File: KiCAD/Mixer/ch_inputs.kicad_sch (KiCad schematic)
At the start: 0 parts

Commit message: Power Bus, Footprints, Audio Bus
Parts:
- added J1: AudioJack2, Eigene:TRS-BHT 3,5mm, symbol Connector_Audio:AudioJack2
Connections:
- net inputs_out: now also J1.T
- new net GND: J1.S

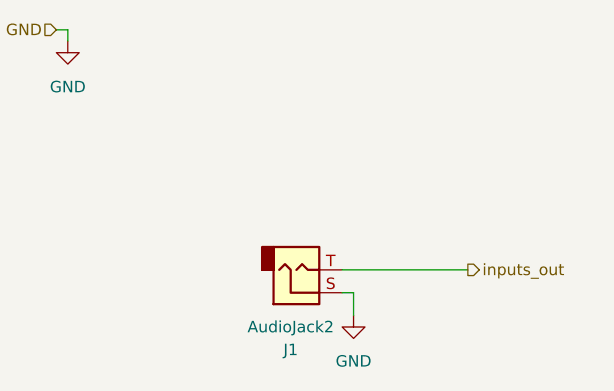
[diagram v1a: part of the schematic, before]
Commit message: added second channel and footprints / created PCB desing...might make PCB bit bigger
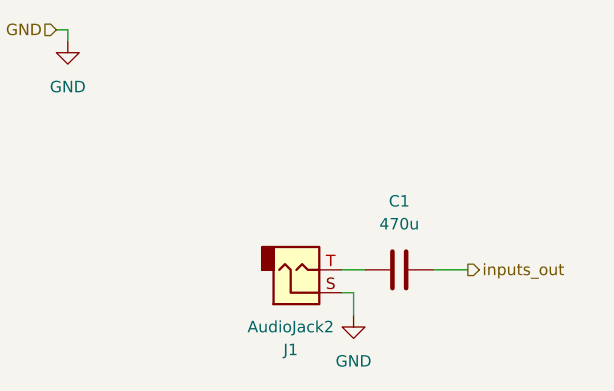
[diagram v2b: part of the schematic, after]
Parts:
- added C1: 470u, Capacitor_SMD:C_0805_2012Metric_Pad1.18x1.45mm_HandSolder, symbol Device:C
- J1: footprint Eigene:TRS-BHT 3,5mm -> Connector_Audio:Jack_3.5mm_QingPu_WQP-PJ398SM_Vertical_CircularHoles
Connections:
- net inputs_out: now also C1.2; no longer J1.T
- new net: C1.1, J1.T
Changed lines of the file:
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@@
 	(wire
 		(pts
-			(xy 58.42 50.8) (xy 72.39 50.8)
+			(xy 58.42 50.8) (xy 60.96 50.8)
 		)
 		(stroke
@@
 		(pts
 			(xy 27.94 24.13) (xy 27.94 25.4)
+		)
+		(stroke
+			(width 0)
+			(type default)
+		)
+	)
+	(wire
+		(pts
+			(xy 68.58 50.8) (xy 72.39 50.8)
 		)
 		(stroke
@@
 			)
 		)
-		(property "Footprint" "Eigene:TRS-BHT 3,5mm"
+		(property "Footprint" "Connector_Audio:Jack_3.5mm_QingPu_WQP-PJ398SM_Vertical_CircularHoles"
 			(at 53.34 50.8 0)
 			(hide yes)
@@
 		(instances
 			(project "Mixer"
+				(path "/322d427a-6aae-4762-92d6-d97688daf29b/8a2849b7-184d-4014-bb98-da9dec8b5f90/1134652d-8354-4f6a-9b2f-dc88b7881384"
+					(reference "J5")
+					(unit 1)
+				)
 				(path "/322d427a-6aae-4762-92d6-d97688daf29b/8a2849b7-184d-4014-bb98-da9dec8b5f90/ec5da5cc-7c1b-4e14-ac3c-00357a5f573e"
 					(reference "J1")
@@
 		(instances
 			(project "Mixer"
+				(path "/322d427a-6aae-4762-92d6-d97688daf29b/8a2849b7-184d-4014-bb98-da9dec8b5f90/1134652d-8354-4f6a-9b2f-dc88b7881384"
+					(reference "#PWR076")
+					(unit 1)
+				)
 				(path "/322d427a-6aae-4762-92d6-d97688daf29b/8a2849b7-184d-4014-bb98-da9dec8b5f90/ec5da5cc-7c1b-4e14-ac3c-00357a5f573e"
 					(reference "#PWR06")
+					(unit 1)
+				)
+			)
+		)
+	)
+	(symbol
+		(lib_id "Device:C")
+		(at 64.77 50.8 90)
+		(unit 1)
+		(body_style 1)
+		(exclude_from_sim no)
+		(in_bom yes)
+		(on_board yes)
+		(in_pos_files yes)
+		(dnp no)
+		(fields_autoplaced yes)
+		(property "Reference" "C1"
+			(at 64.77 43.18 90)
+			(show_name no)
+			(do_not_autoplace no)
+			(effects
+				(font
+					(size 1.27 1.27)
+				)
+			)
+		)
+		(property "Value" "470u"
+			(at 64.77 45.72 90)
+			(show_name no)
+			(do_not_autoplace no)
+			(effects
+				(font
+					(size 1.27 1.27)
+				)
+			)
+		)
+		(property "Footprint" "Capacitor_SMD:C_0805_2012Metric_Pad1.18x1.45mm_HandSolder"
+			(at 68.58 49.8348 0)
+			(hide yes)
+			(show_name no)
+			(do_not_autoplace no)
+			(effects
+				(font
+					(size 1.27 1.27)
+				)
+			)
+		)
+		(property "Datasheet" ""
+			(at 64.77 50.8 0)
+			(hide yes)
+			(show_name no)
+			(do_not_autoplace no)
+			(effects
+				(font
+					(size 1.27 1.27)
+				)
+			)
+		)
+		(property "Description" "Unpolarized capacitor"
+			(at 64.77 50.8 0)
+			(hide yes)
+			(show_name no)
+			(do_not_autoplace no)
+			(effects
+				(font
+					(size 1.27 1.27)
+				)
+			)
+		)
+		(pin "1"
+		)
+		(pin "2"
+		)
+		(instances
+			(project "Mixer"
+				(path "/322d427a-6aae-4762-92d6-d97688daf29b/8a2849b7-184d-4014-bb98-da9dec8b5f90/1134652d-8354-4f6a-9b2f-dc88b7881384"
+					(reference "C3")
+					(unit 1)
+				)
+				(path "/322d427a-6aae-4762-92d6-d97688daf29b/8a2849b7-184d-4014-bb98-da9dec8b5f90/ec5da5cc-7c1b-4e14-ac3c-00357a5f573e"
+					(reference "C1")
 					(unit 1)
 				)
@@
 		(instances
 			(project "Mixer"
+				(path "/322d427a-6aae-4762-92d6-d97688daf29b/8a2849b7-184d-4014-bb98-da9dec8b5f90/1134652d-8354-4f6a-9b2f-dc88b7881384"
+					(reference "#PWR075")
+					(unit 1)
+				)
 				(path "/322d427a-6aae-4762-92d6-d97688daf29b/8a2849b7-184d-4014-bb98-da9dec8b5f90/ec5da5cc-7c1b-4e14-ac3c-00357a5f573e"
 					(reference "#PWR035")

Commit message: überarbeitete Schaltung und PCB Desing...v1.0 FERTIG
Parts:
- added R11: R, Resistor_SMD:R_0805_2012Metric_Pad1.20x1.40mm_HandSolder, symbol Device:R
- C1: value 470u -> 4,7
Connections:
- net GND: now also R11.1
- net inputs_out: now also R11.2
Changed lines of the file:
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@@
 	(generator_version "10.0")
 	(paper "A4")
-	(wire
-		(pts
-			(xy 59.69 53.34) (xy 59.69 55.88)
+	(junction
+		(at 59.69 58.42)
+		(diameter 0)
+		(color 0 0 0 0)
+	)
+	(junction
+		(at 71.12 50.8)
+		(diameter 0)
+		(color 0 0 0 0)
+	)
+	(wire
+		(pts
+			(xy 59.69 53.34) (xy 59.69 58.42)
+		)
+		(stroke
+			(width 0)
+			(type default)
+		)
+	)
+	(wire
+		(pts
+			(xy 71.12 50.8) (xy 82.55 50.8)
+		)
+		(stroke
+			(width 0)
+			(type default)
+		)
+	)
+	(wire
+		(pts
+			(xy 59.69 58.42) (xy 59.69 68.58)
 		)
 		(stroke
@@
 	(wire
 		(pts
-			(xy 27.94 24.13) (xy 27.94 25.4)
-		)
-		(stroke
-			(width 0)
-			(type default)
-		)
-	)
-	(wire
-		(pts
-			(xy 68.58 50.8) (xy 72.39 50.8)
-		)
-		(stroke
-			(width 0)
-			(type default)
-		)
-	)
-	(wire
-		(pts
-			(xy 26.67 24.13) (xy 27.94 24.13)
+			(xy 59.69 58.42) (xy 71.12 58.42)
+		)
+		(stroke
+			(width 0)
+			(type default)
+		)
+	)
+	(wire
+		(pts
+			(xy 68.58 50.8) (xy 71.12 50.8)
 		)
 		(stroke
@@
 	(hierarchical_label "GND"
 		(shape input)
-		(at 26.67 24.13 180)
+		(at 59.69 68.58 180)
 		(effects
 			(font
@@
 	(hierarchical_label "inputs_out"
 		(shape output)
-		(at 72.39 50.8 0)
+		(at 82.55 50.8 0)
 		(effects
 			(font
@@
 	)
 	(symbol
-		(lib_id "power:GND")
-		(at 59.69 55.88 0)
+		(lib_id "Device:R")
+		(at 71.12 54.61 180)
 		(unit 1)
 		(body_style 1)
@@
 		(dnp no)
 		(fields_autoplaced yes)
-		(property "Reference" "#PWR06"
-			(at 59.69 62.23 0)
-			(hide yes)
-			(show_name no)
-			(do_not_autoplace no)
-			(effects
-				(font
-					(size 1.27 1.27)
-				)
-			)
-		)
-		(property "Value" "GND"
-			(at 59.69 60.96 0)
-			(show_name no)
-			(do_not_autoplace no)
-			(effects
-				(font
-					(size 1.27 1.27)
-				)
-			)
-		)
-		(property "Footprint" ""
-			(at 59.69 55.88 0)
+		(property "Reference" "R11"
+			(at 73.66 53.34 0)
+			(show_name no)
+			(do_not_autoplace no)
+			(effects
+				(font
+					(size 1.27 1.27)
+				)
+				(justify right)
+			)
+		)
+		(property "Value" "R"
+			(at 73.66 55.88 0)
+			(show_name no)
+			(do_not_autoplace no)
+			(effects
+				(font
+					(size 1.27 1.27)
+				)
+				(justify right)
+			)
+		)
+		(property "Footprint" "Resistor_SMD:R_0805_2012Metric_Pad1.20x1.40mm_HandSolder"
+			(at 72.898 54.61 90)
 			(hide yes)
 			(show_name no)
@@
 		)
 		(property "Datasheet" ""
-			(at 59.69 55.88 0)
-			(hide yes)
-			(show_name no)
-			(do_not_autoplace no)
-			(effects
-				(font
-					(size 1.27 1.27)
-				)
-			)
-		)
-		(property "Description" "Power symbol creates a global label with name \"GND\" , ground"
-			(at 59.69 55.88 0)
+			(at 71.12 54.61 0)
+			(hide yes)
+			(show_name no)
+			(do_not_autoplace no)
+			(effects
+				(font
+					(size 1.27 1.27)
+				)
+			)
+		)
+		(property "Description" "Resistor"
+			(at 71.12 54.61 0)
 			(hide yes)
 			(show_name no)
@@
 		)
 		(pin "1"
+		)
+		(pin "2"
 		)
 		(instances
 			(project "Mixer"
 				(path "/322d427a-6aae-4762-92d6-d97688daf29b/8a2849b7-184d-4014-bb98-da9dec8b5f90/1134652d-8354-4f6a-9b2f-dc88b7881384"
-					(reference "#PWR076")
+					(reference "R12")
 					(unit 1)
 				)
 				(path "/322d427a-6aae-4762-92d6-d97688daf29b/8a2849b7-184d-4014-bb98-da9dec8b5f90/ec5da5cc-7c1b-4e14-ac3c-00357a5f573e"
-					(reference "#PWR06")
+					(reference "R11")
 					(unit 1)
 				)
@@
 			)
 		)
-		(property "Value" "470u"
+		(property "Value" "4,7"
 			(at 64.77 45.72 90)
 			(show_name no)
@@
 					(unit 1)
 				)
-			)
-		)
-	)
-	(symbol
-		(lib_id "power:GND")
-		(at 27.94 25.4 0)
-		(unit 1)
-		(body_style 1)
-		(exclude_from_sim no)
-		(in_bom yes)
-		(on_board yes)
-		(in_pos_files yes)
-		(dnp no)
-		(fields_autoplaced yes)
-		(property "Reference" "#PWR035"
-			(at 27.94 31.75 0)
-			(hide yes)
-			(show_name no)
-			(do_not_autoplace no)
-			(effects
-				(font
-					(size 1.27 1.27)
-				)
-			)
-		)
-		(property "Value" "GND"
-			(at 27.94 30.48 0)
-			(show_name no)
-			(do_not_autoplace no)
-			(effects
-				(font
-					(size 1.27 1.27)
-				)
-			)
-		)
-		(property "Footprint" ""
-			(at 27.94 25.4 0)
-			(hide yes)
-			(show_name no)
-			(do_not_autoplace no)
-			(effects
-				(font
-					(size 1.27 1.27)
-				)
-			)
-		)
-		(property "Datasheet" ""
-			(at 27.94 25.4 0)
-			(hide yes)
-			(show_name no)
-			(do_not_autoplace no)
-			(effects
-				(font
-					(size 1.27 1.27)
-				)
-			)
-		)
-		(property "Description" "Power symbol creates a global label with name \"GND\" , ground"
-			(at 27.94 25.4 0)
-			(hide yes)
-			(show_name no)
-			(do_not_autoplace no)
-			(effects
-				(font
-					(size 1.27 1.27)
-				)
-			)
-		)
-		(pin "1"
-		)
-		(instances
-			(project "Mixer"
-				(path "/322d427a-6aae-4762-92d6-d97688daf29b/8a2849b7-184d-4014-bb98-da9dec8b5f90/1134652d-8354-4f6a-9b2f-dc88b7881384"
-					(reference "#PWR075")
-					(unit 1)
-				)
-				(path "/322d427a-6aae-4762-92d6-d97688daf29b/8a2849b7-184d-4014-bb98-da9dec8b5f90/ec5da5cc-7c1b-4e14-ac3c-00357a5f573e"
-					(reference "#PWR035")
-					(unit 1)
-				)
